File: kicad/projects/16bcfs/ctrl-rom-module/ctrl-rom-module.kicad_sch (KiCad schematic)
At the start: 32 parts, among them J1 Address Pins, J2 Signal Pins, J3 Control Pins, U1 25LCxxx, U2 AS6C62256, U3 74HC164, U4 74HC574, U5 74HC541, U6 74HC541

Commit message: Control ROM PCB Layout (#131)
* Closes #118
* Fixes #126
* Fixes #127
* Closes #128
* Closes #129
* Starts #119
* Closes #125

Co-authored-by: Adam Clark <adam@eryjus.com>
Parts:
- added C8: 47u, Capacitor_SMD:C_1206_3216Metric_Pad1.33x1.80mm_HandSolder, symbol Device:C
- C1, C2, C3, C4, C5, C6, C7: footprint (none) -> Capacitor_SMD:C_1206_3216Metric_Pad1.33x1.80mm_HandSolder
- D1, D2, D3, D4, D5, D6, D7, D8: footprint (none) -> LED_SMD:LED_1206_3216Metric_Pad1.42x1.75mm_HandSolder
- J1, J3: footprint (none) -> Connector_PinHeader_2.54mm:PinHeader_1x16_P2.54mm_Vertical
- J2: footprint (none) -> Connector_PinHeader_2.54mm:PinHeader_1x08_P2.54mm_Vertical
- R1, R2, R3, R4, R5, R6, R7, R8: footprint (none) -> Resistor_SMD:R_1206_3216Metric_Pad1.30x1.75mm_HandSolder
- U1: footprint (none) -> Package_DIP:DIP-8_W7.62mm_Socket
- U2: footprint Package_DIP:DIP-28_W15.24mm -> eryjus:SOP-28_MIL330_ALL
- U3: footprint (none) -> Package_SO:SOIC-14_3.9x8.7mm_P1.27mm
- U4, U5, U6: footprint (none) -> Package_SO:SOIC-20W_7.5x12.8mm_P1.27mm
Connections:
- net GNDREF: now also C8.2
- net VCC: now also C8.1
- net CLK renamed CPU_CLK
- net Qc renamed LATCH ~{OE}
- net ~{Qc} renamed SHIFTER ~{OE}
- net ~{Qr} renamed SHIFTER ~{RESET}

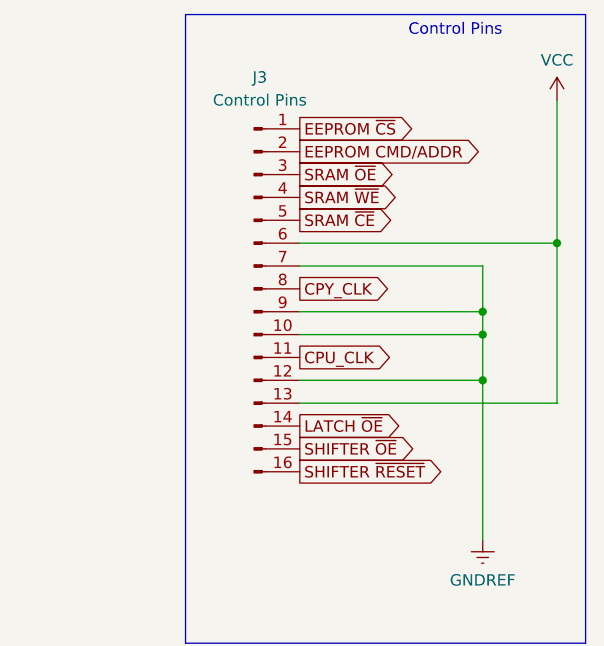
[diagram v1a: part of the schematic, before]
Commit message: Update the directive prefixes to be '.', ':', or '%' as appropriate.
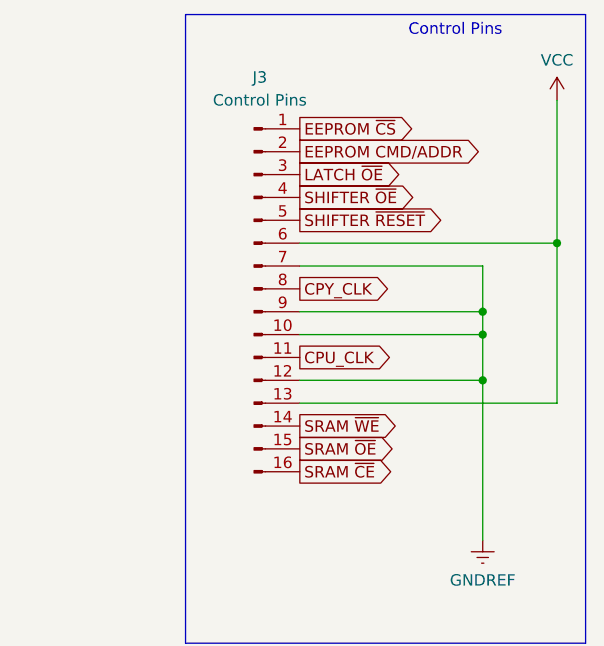
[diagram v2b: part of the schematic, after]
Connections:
- net LATCH ~{OE}: now also J3.3 (Pin_3); no longer J3.14 (Pin_14)
- net SHIFTER ~{OE}: now also J3.4 (Pin_4); no longer J3.15 (Pin_15)
- net SHIFTER ~{RESET}: now also J3.5 (Pin_5); no longer J3.16 (Pin_16)
- net SRAM ~{CE}: now also J3.16 (Pin_16); no longer J3.5 (Pin_5)
- net SRAM ~{OE}: now also J3.15 (Pin_15); no longer J3.3 (Pin_3)
- net SRAM ~{WE}: now also J3.14 (Pin_14); no longer J3.4 (Pin_4)
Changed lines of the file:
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@@
     )
   )
-  (global_label "SRAM ~{OE}" (shape output) (at 379.095 159.385 0) (fields_autoplaced)
-    (effects (font (size 1.27 1.27)) (justify left))
-    (property "Intersheetrefs" "${INTERSHEET_REFS}" (at 390.5468 159.385 0)
+  (global_label "SRAM ~{OE}" (shape output) (at 379.095 189.865 0) (fields_autoplaced)
+    (effects (font (size 1.27 1.27)) (justify left))
+    (property "Intersheetrefs" "${INTERSHEET_REFS}" (at 390.5468 189.865 0)
       (effects (font (size 1.27 1.27)) (justify left) hide)
     )
@@
     )
   )
-  (global_label "SHIFTER ~{OE}" (shape output) (at 379.095 189.865 0) (fields_autoplaced)
-    (effects (font (size 1.27 1.27)) (justify left))
-    (property "Intersheetrefs" "${INTERSHEET_REFS}" (at 393.1473 189.865 0)
+  (global_label "SHIFTER ~{OE}" (shape output) (at 379.095 161.925 0) (fields_autoplaced)
+    (effects (font (size 1.27 1.27)) (justify left))
+    (property "Intersheetrefs" "${INTERSHEET_REFS}" (at 393.1473 161.925 0)
       (effects (font (size 1.27 1.27)) (justify left) hide)
     )
@@
     )
   )
-  (global_label "SRAM ~{CE}" (shape output) (at 379.095 164.465 0) (fields_autoplaced)
-    (effects (font (size 1.27 1.27)) (justify left))
-    (property "Intersheetrefs" "${INTERSHEET_REFS}" (at 390.4863 164.465 0)
+  (global_label "SRAM ~{CE}" (shape output) (at 379.095 192.405 0) (fields_autoplaced)
+    (effects (font (size 1.27 1.27)) (justify left))
+    (property "Intersheetrefs" "${INTERSHEET_REFS}" (at 390.4863 192.405 0)
       (effects (font (size 1.27 1.27)) (justify left) hide)
     )
@@
     )
   )
-  (global_label "SRAM ~{WE}" (shape output) (at 379.095 161.925 0) (fields_autoplaced)
-    (effects (font (size 1.27 1.27)) (justify left))
-    (property "Intersheetrefs" "${INTERSHEET_REFS}" (at 390.6677 161.925 0)
+  (global_label "SRAM ~{WE}" (shape output) (at 379.095 187.325 0) (fields_autoplaced)
+    (effects (font (size 1.27 1.27)) (justify left))
+    (property "Intersheetrefs" "${INTERSHEET_REFS}" (at 390.6677 187.325 0)
       (effects (font (size 1.27 1.27)) (justify left) hide)
     )
@@
     )
   )
-  (global_label "SHIFTER ~{RESET}" (shape output) (at 379.095 192.405 0) (fields_autoplaced)
-    (effects (font (size 1.27 1.27)) (justify left))
-    (property "Intersheetrefs" "${INTERSHEET_REFS}" (at 396.4129 192.405 0)
+  (global_label "SHIFTER ~{RESET}" (shape output) (at 379.095 164.465 0) (fields_autoplaced)
+    (effects (font (size 1.27 1.27)) (justify left))
+    (property "Intersheetrefs" "${INTERSHEET_REFS}" (at 396.4129 164.465 0)
       (effects (font (size 1.27 1.27)) (justify left) hide)
     )
@@
     )
   )
-  (global_label "LATCH ~{OE}" (shape output) (at 379.095 187.325 0) (fields_autoplaced)
-    (effects (font (size 1.27 1.27)) (justify left))
-    (property "Intersheetrefs" "${INTERSHEET_REFS}" (at 391.2121 187.325 0)
-      (effects (font (size 1.27 1.27)) (justify left) hide)
-    )
+  (global_label "LATCH ~{OE}" (shape output) (at 379.095 159.385 0) (fields_autoplaced)
+    (effects (font (size 1.27 1.27)) (justify left))
+    (property "Intersheetrefs" "${INTERSHEET_REFS}" (at 391.2121 159.385 0)
+      (effects (font (size 1.27 1.27)) (justify left) hide)
+    )
